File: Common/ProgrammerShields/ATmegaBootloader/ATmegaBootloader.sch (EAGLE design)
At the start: 6 parts, among them J1 ARDUINO_R3_SHIELD

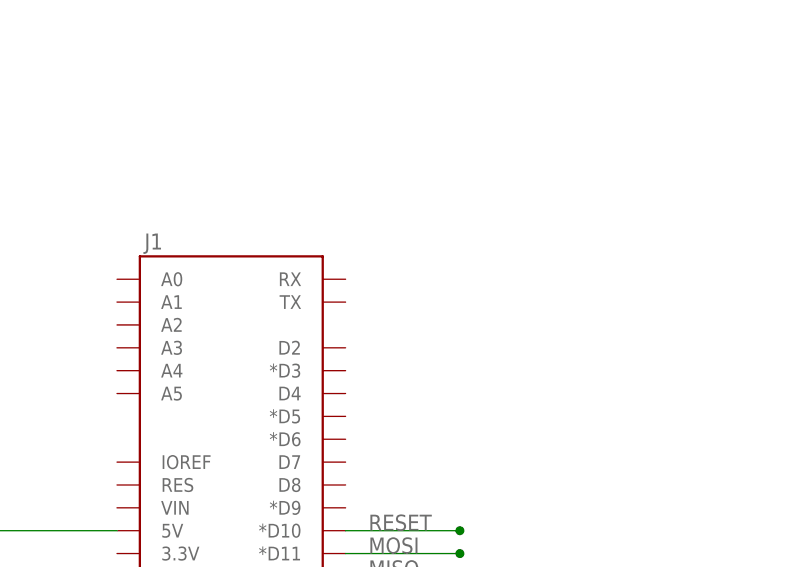
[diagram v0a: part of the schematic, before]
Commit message: renamed our Arduino Shields folder
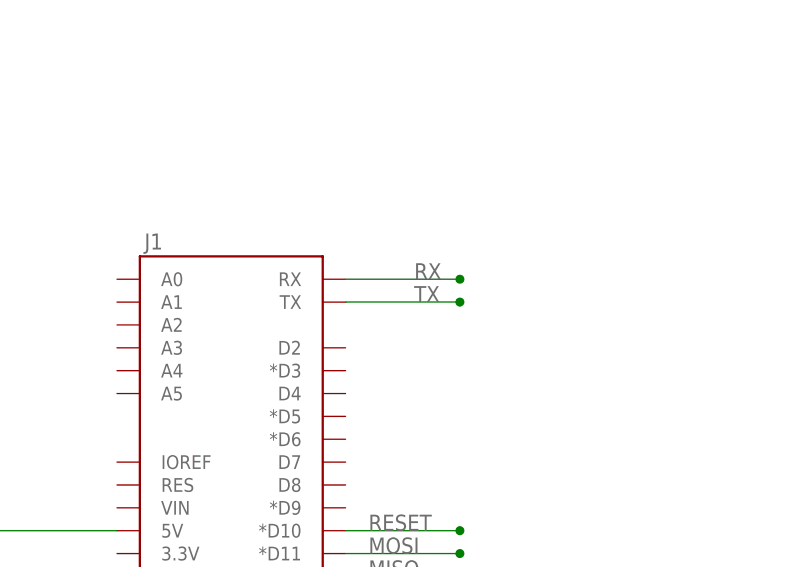
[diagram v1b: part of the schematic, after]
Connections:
- new net RX: J1.RX
- new net TX: J1.TX
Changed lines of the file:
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@@
+</segment>
+</net>
+<net name="RX" class="0">
+<segment>
+<pinref part="J1" gate="G$1" pin="RX"/>
+<wire x1="12.7" y1="17.78" x2="25.4" y2="17.78" width="0.1524" layer="91"/>
+<junction x="25.4" y="17.78"/>
+<label x="20.32" y="17.78" size="1.778" layer="95"/>
+</segment>
+</net>
+<net name="TX" class="0">
+<segment>
+<pinref part="J1" gate="G$1" pin="TX"/>
+<wire x1="12.7" y1="15.24" x2="25.4" y2="15.24" width="0.1524" layer="91"/>
+<junction x="25.4" y="15.24"/>
+<label x="20.32" y="15.24" size="1.778" layer="95"/>
 </segment>
 </net>

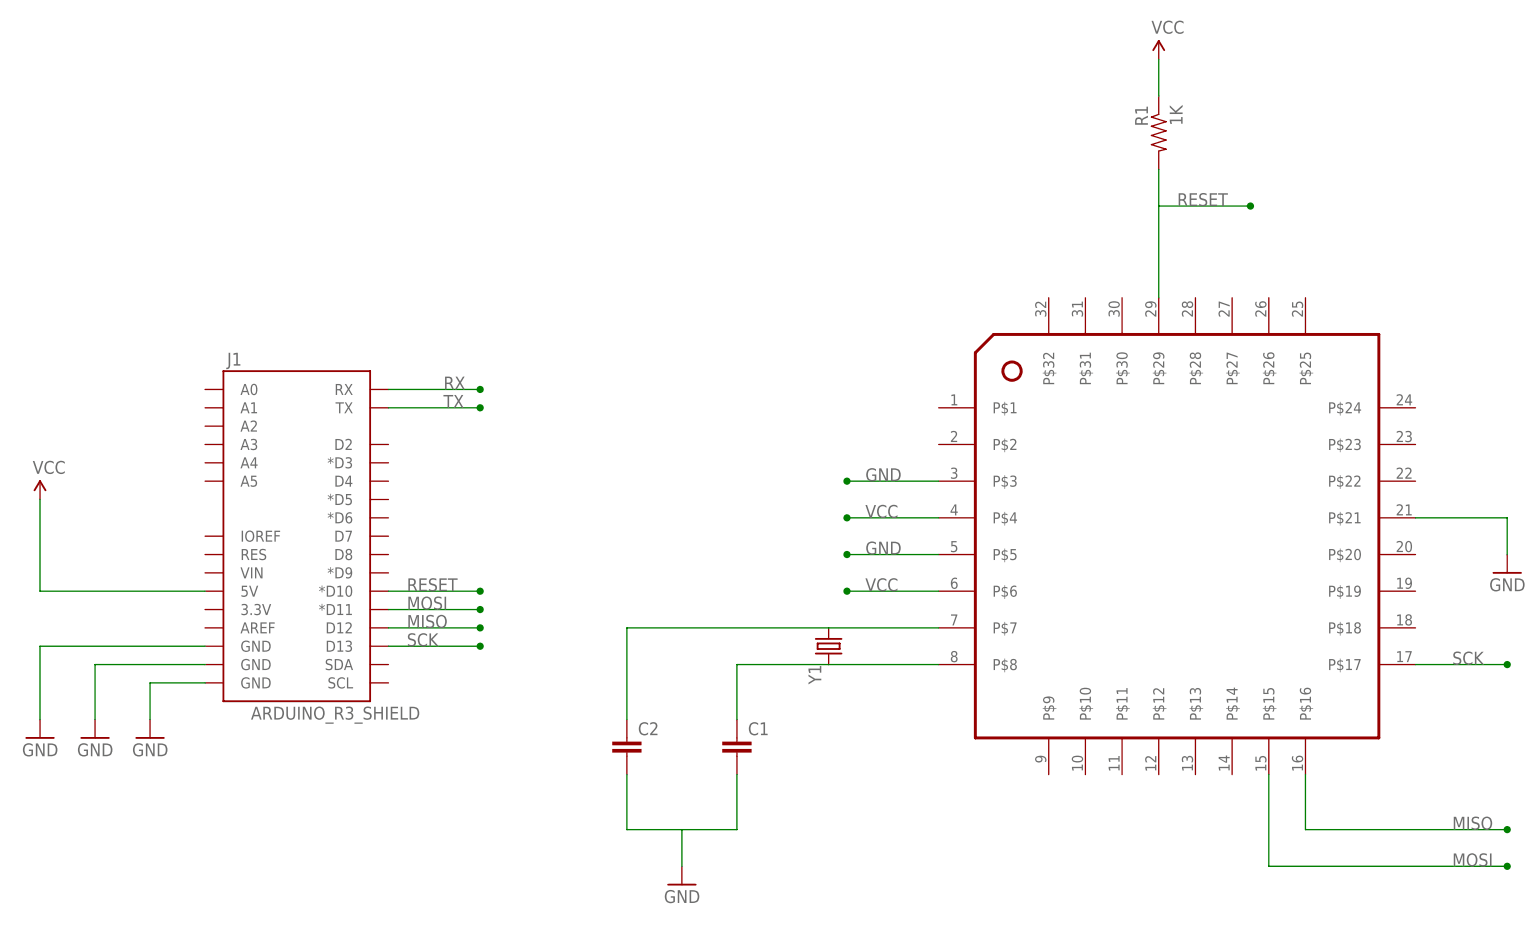
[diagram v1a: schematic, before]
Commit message: Changed Schematic for ATmega programming shield
Added switch so board can be used for programming the bootloader and
normal programs
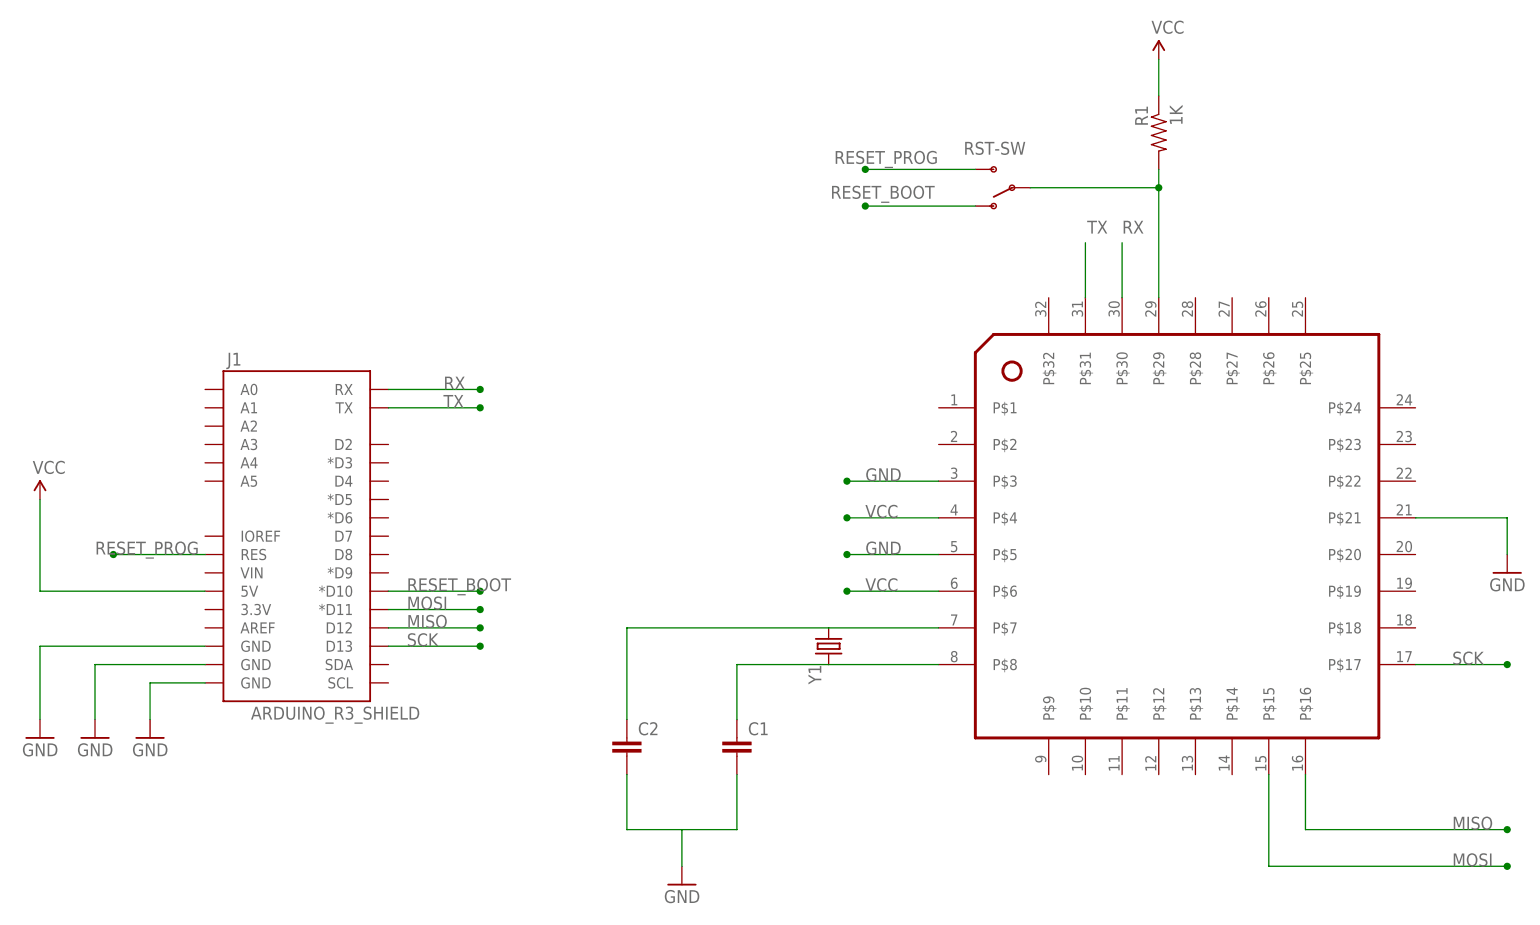
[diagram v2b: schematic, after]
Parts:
- added RST-SW: (no value), SparkFun-Electromechanical:SWITCH-SPDTPTH
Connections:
- new net RESET_BOOT: J1.*D10, RST-SW.O
- new net RESET_PROG: J1.RES, RST-SW.S
- net RESET: now also RST-SW.P; no longer J1.*D10
- net RX: now also U$1.P$30
- net TX: now also U$1.P$31
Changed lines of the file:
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@@
 <?xml version="1.0" encoding="utf-8"?>
 <!DOCTYPE eagle SYSTEM "eagle.dtd">
-<eagle version="7.3.0">
+<eagle version="7.6.0">
 <drawing>
 <settings>
@@
 <part name="SUPPLY2" library="SparkFun-Aesthetics" deviceset="VCC" device=""/>
 <part name="GND5" library="SparkFun-Aesthetics" deviceset="GND" device=""/>
+<part name="RST-SW" library="SparkFun-Electromechanical" deviceset="SWITCH-SPDT" device="PTH"/>
 </parts>
 <sheets>
@@
 <instance part="SUPPLY2" gate="G$1" x="-35.56" y="2.54"/>
 <instance part="GND5" gate="1" x="53.34" y="-50.8" rot="MR0"/>
+<instance part="RST-SW" gate="1" x="99.06" y="45.72" rot="R180"/>
 </instances>
 <busses>
@@
 <segment>
 <pinref part="U$1" gate="G$1" pin="P$29"/>
-<wire x1="119.38" y1="30.48" x2="119.38" y2="43.18" width="0.1524" layer="91"/>
-<wire x1="119.38" y1="43.18" x2="132.08" y2="43.18" width="0.1524" layer="91"/>
-<label x="121.92" y="43.18" size="1.778" layer="95"/>
-<junction x="132.08" y="43.18"/>
+<wire x1="119.38" y1="30.48" x2="119.38" y2="45.72" width="0.1524" layer="91"/>
 <pinref part="R1" gate="G$1" pin="2"/>
-<wire x1="119.38" y1="43.18" x2="119.38" y2="48.26" width="0.1524" layer="91"/>
-</segment>
-<segment>
-<pinref part="J1" gate="G$1" pin="*D10"/>
-<wire x1="12.7" y1="-10.16" x2="25.4" y2="-10.16" width="0.1524" layer="91"/>
-<label x="15.24" y="-10.16" size="1.778" layer="95"/>
-<junction x="25.4" y="-10.16"/>
+<wire x1="119.38" y1="45.72" x2="119.38" y2="48.26" width="0.1524" layer="91"/>
+<wire x1="119.38" y1="45.72" x2="101.6" y2="45.72" width="0.1524" layer="91"/>
+<junction x="119.38" y="45.72"/>
+<pinref part="RST-SW" gate="1" pin="P"/>
 </segment>
 </net>
@@
 <label x="20.32" y="17.78" size="1.778" layer="95"/>
 </segment>
+<segment>
+<pinref part="U$1" gate="G$1" pin="P$30"/>
+<wire x1="114.3" y1="38.1" x2="114.3" y2="30.48" width="0.1524" layer="91"/>
+<label x="114.3" y="39.37" size="1.778" layer="95"/>
+</segment>
 </net>
 <net name="TX" class="0">
@@
 <label x="20.32" y="15.24" size="1.778" layer="95"/>
 </segment>
-</net>
+<segment>
+<pinref part="U$1" gate="G$1" pin="P$31"/>
+<wire x1="109.22" y1="38.1" x2="109.22" y2="30.48" width="0.1524" layer="91"/>
+<label x="109.474" y="39.37" size="1.778" layer="95"/>
+</segment>
+</net>
+<net name="RESET_BOOT" class="0">
+<segment>
+<pinref part="J1" gate="G$1" pin="*D10"/>
+<wire x1="12.7" y1="-10.16" x2="25.4" y2="-10.16" width="0.1524" layer="91"/>
+<label x="15.24" y="-10.16" size="1.778" layer="95"/>
+<junction x="25.4" y="-10.16"/>
+</segment>
+<segment>
+<pinref part="RST-SW" gate="1" pin="O"/>
+<wire x1="93.98" y1="43.18" x2="78.74" y2="43.18" width="0.1524" layer="91"/>
+<label x="73.914" y="44.196" size="1.778" layer="95"/>
+<junction x="78.74" y="43.18"/>
+</segment>
+</net>
+<net name="RESET_PROG" class="0">
+<segment>
+<pinref part="J1" gate="G$1" pin="RES"/>
+<wire x1="-12.7" y1="-5.08" x2="-25.4" y2="-5.08" width="0.1524" layer="91"/>
+<label x="-27.94" y="-5.08" size="1.778" layer="95"/>
+<junction x="-25.4" y="-5.08"/>
+</segment>
+<segment>
+<pinref part="RST-SW" gate="1" pin="S"/>
+<wire x1="93.98" y1="48.26" x2="78.74" y2="48.26" width="0.1524" layer="91"/>
+<label x="74.422" y="49.022" size="1.778" layer="95"/>
+<junction x="78.74" y="48.26"/>
+</segment>
+</net>
